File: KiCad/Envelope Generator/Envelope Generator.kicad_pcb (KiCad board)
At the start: 2 copper layers, 66 parts, among them J1 Screw_Terminal_01x03, J2 Screw_Terminal_01x03, U1 TL074, U2 TL074, U3 TL074

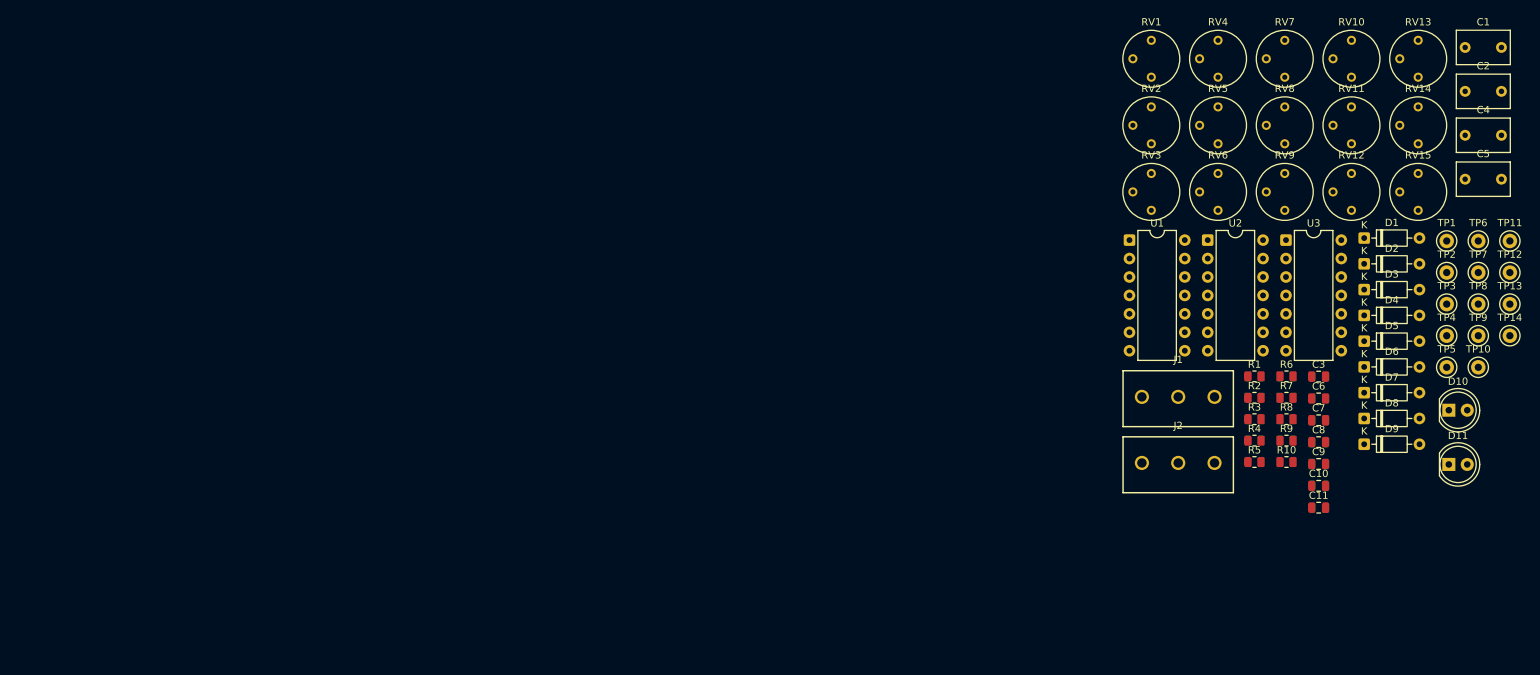
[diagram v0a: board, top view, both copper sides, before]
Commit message: envelope generator pcb layout done
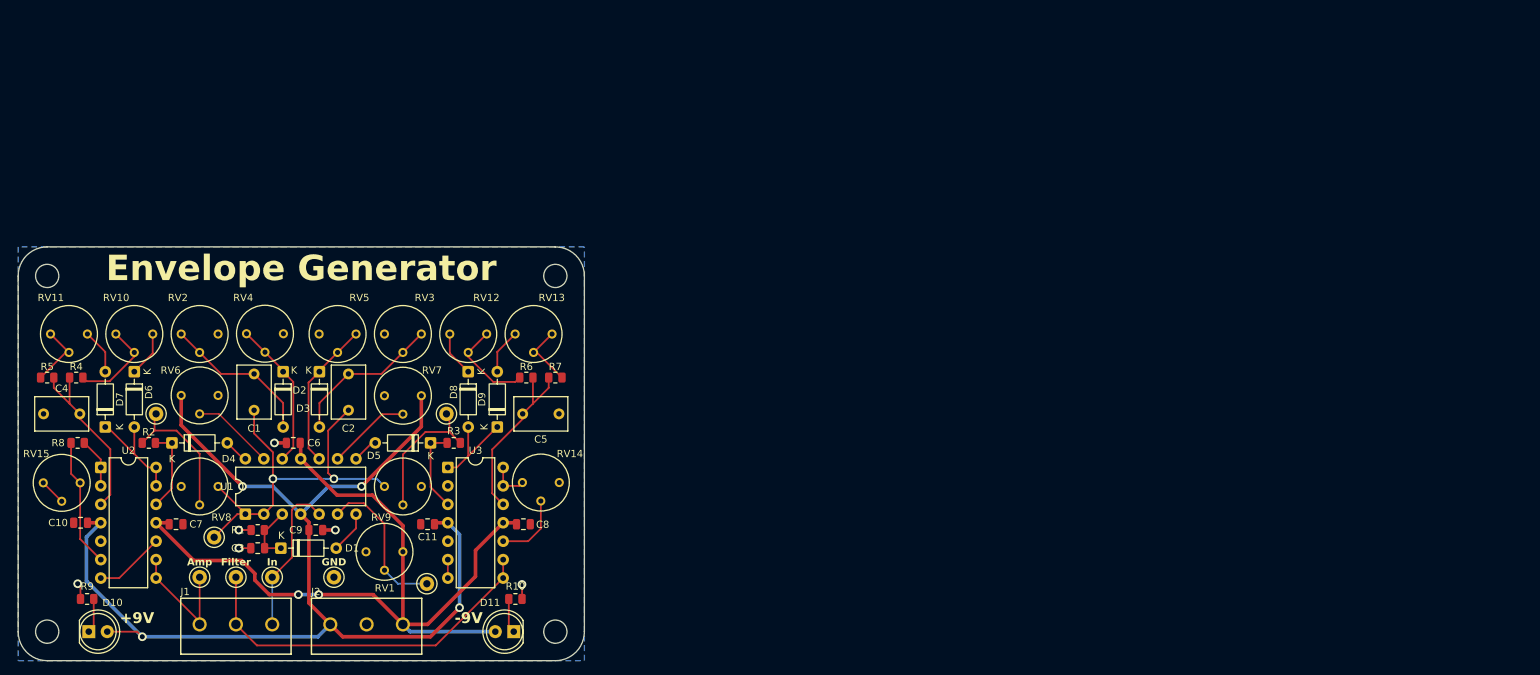
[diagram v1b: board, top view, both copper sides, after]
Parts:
- removed TP10, TP11, TP13, TP14, TP2, TP3: TestPoint_Small, TestPoint:TestPoint_Keystone_5000-5004_Miniature
- added H1: MountingHole, MountingHole:MountingHole_3.2mm_M3, F.Cu at (18.0, 66.0)
- added H2: MountingHole, MountingHole:MountingHole_3.2mm_M3, F.Cu at (18.0, 115.0)
- added H3: MountingHole, MountingHole:MountingHole_3.2mm_M3, F.Cu at (88.0, 115.0)
- added H4: MountingHole, MountingHole:MountingHole_3.2mm_M3, F.Cu at (88.0, 66.0)
- R10, R9: value R_US -> 1k
- moved C4 199.5 mm to (17.5, 85.0)
- moved D10 189.8 mm to (23.7, 115.0)
- moved RV15 188.1 mm to (22.5, 94.5), turned to 90 degrees
- moved TP7 181.1 mm to (39.0, 107.5)
- moved TP5 177.9 mm to (33.0, 85.0)
- moved RV11 176.1 mm to (23.5, 74.0), turned to 90 degrees
- moved TP8 175.2 mm to (44.0, 107.5)
- moved C1 174.1 mm to (46.5, 84.5), turned to 90 degrees
- moved D7 173.5 mm to (26.0, 86.8), turned to 90 degrees
- moved TP4 172.0 mm to (41.0, 102.0)
- moved C10 170.6 mm to (22.6, 100.0)
- moved TP9 169.4 mm to (49.0, 107.5)
- moved D6 169.4 mm to (30.0, 79.2), turned to -90 degrees
- moved RV10 168.9 mm to (32.5, 74.0), turned to 90 degrees
- moved TP12 167.3 mm to (57.5, 107.5)
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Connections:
- C4 pad 2: Net-(U2C-+) -> Net-(U2A-+)
- C5 pad 2: Net-(U2B-+) -> Net-(U3D-+)
- D11 pad 2: GND -> -9V
- J1 pad 1: /Envelope Generator/In -> /Envelope Generator/Amp Out
- J1 pad 2: /Envelope Generator/Amp Out -> /Envelope Generator/Filter Out
- J1 pad 3: /Envelope Generator/Filter Out -> /Envelope Generator/In
- R10 pad 2: -9V -> GND
- R4 pad 2: Net-(U2C-+) -> Net-(U2A-+)
- R5 pad 2: Net-(U2C-+) -> Net-(U2A-+)
- R6 pad 2: Net-(U2B-+) -> Net-(U3D-+)
- R7 pad 2: Net-(U2B-+) -> Net-(U3D-+)
- R8 pad 2: Net-(U3D--) -> Net-(U2B--)
- RV12 pad 1: Net-(D8-K) -> Net-(R6-Pad1)
- RV12 pad 3: Net-(R6-Pad1) -> Net-(D8-K)
- RV13 pad 1: Net-(D9-A) -> Net-(R7-Pad1)
- RV13 pad 3: Net-(R7-Pad1) -> Net-(D9-A)
- RV14 pad 1: /Envelope Generator/Unscaled Filter Out -> GND
- RV14 pad 2: Net-(U3B-+) -> Net-(U3C-+)
- RV14 pad 3: GND -> /Envelope Generator/Unscaled Filter Out
- RV15 pad 1: Net-(U3D--) -> Net-(U2B--)
- RV15 pad 2: Net-(U3C-+) -> Net-(U2C-+)
- RV15 pad 3: Net-(U3C-+) -> Net-(U2C-+)
- RV2 pad 1: Net-(D2-A) -> GND
- RV2 pad 3: GND -> Net-(D2-A)
- RV4 pad 1: Net-(D2-K) -> GND
- RV4 pad 3: GND -> Net-(D2-K)
- RV6 pad 1: +9V -> GND
- RV6 pad 2: Net-(U1C--) -> Net-(U1D--)
- RV6 pad 3: GND -> +9V
- RV7 pad 2: Net-(U1B--) -> Net-(U1C--)
- RV9 pad 1: /Envelope Generator/Normalized In -> GND
- RV9 pad 3: GND -> /Envelope Generator/Normalized In
- TP12 pad 1: /Envelope Generator/Unscaled Amp Out -> GND
- TP7 pad 1: /Envelope Generator/Amp Target Voltage -> /Envelope Generator/Amp Out
- TP8 pad 1: /Envelope Generator/Filter Target Voltage -> /Envelope Generator/Filter Out
- U1 pad 1: Net-(D1-A) -> /Envelope Generator/Normalized In
- U1 pad 10: Net-(D2-K) -> Net-(D3-K)
- U1 pad 12: Net-(D1-K) -> Net-(D2-K)
- U1 pad 13: /Envelope Generator/Normalized In -> Net-(U1D--)
- U1 pad 14: /Envelope Generator/Normalized In -> /Envelope Generator/Amp Burst
- U1 pad 2: /Envelope Generator/Input Comparator Ref -> /Envelope Generator/Normalized In
- U1 pad 3: /Envelope Generator/In -> Net-(D1-K)
- U1 pad 5: Net-(D3-K) -> /Envelope Generator/In
- U1 pad 6: Net-(U1B--) -> /Envelope Generator/Input Comparator Ref
- U1 pad 7: /Envelope Generator/Filter Burst -> Net-(D1-A)
- U1 pad 8: /Envelope Generator/Amp Burst -> /Envelope Generator/Filter Burst
- U2 pad 1: /Envelope Generator/Filter Target Voltage -> /Envelope Generator/Unscaled Amp Out
- U2 pad 2: /Envelope Generator/Filter Target Voltage -> /Envelope Generator/Unscaled Amp Out
- U2 pad 3: Net-(D5-K) -> Net-(U2A-+)
- U2 pad 5: Net-(U2B-+) -> GND
- U2 pad 6: /Envelope Generator/Unscaled Filter Out -> Net-(U2B--)
- U2 pad 7: /Envelope Generator/Unscaled Filter Out -> Net-(U2C-+)
- U2 pad 8: /Envelope Generator/Unscaled Amp Out -> /Envelope Generator/Amp Out
- U2 pad 9: /Envelope Generator/Unscaled Amp Out -> /Envelope Generator/Amp Out
- U3 pad 1: /Power/Thaw 3 -> /Envelope Generator/Filter Target Voltage
- U3 pad 12: GND -> Net-(U3D-+)
- U3 pad 13: Net-(U3D--) -> /Envelope Generator/Unscaled Filter Out
- U3 pad 14: Net-(U3C-+) -> /Envelope Generator/Unscaled Filter Out
- U3 pad 2: /Power/Thaw 3 -> /Envelope Generator/Filter Target Voltage
- U3 pad 3: GND -> Net-(D5-K)
- U3 pad 5: Net-(U3B-+) -> GND
- U3 pad 6: /Envelope Generator/Filter Out -> /Power/Thaw 3
- U3 pad 7: /Envelope Generator/Filter Out -> /Power/Thaw 3
- U3 pad 8: /Envelope Generator/Amp Out -> /Envelope Generator/Filter Out
- U3 pad 9: /Envelope Generator/Amp Out -> /Envelope Generator/Filter Out
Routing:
- net +9V: track 0.00 -> 156.1 mm, vias 0 -> 4
- net -9V: track 0.00 -> 112.8 mm, vias 0 -> 2
- net /Envelope Generator/Normalized In: track 0.00 -> 56.2 mm, vias 0 -> 2
- net /Envelope Generator/Filter Out: track 0.00 -> 50.9 mm
- net Net-(U3D-+): track 0.00 -> 24.9 mm
- net Net-(U2A-+): track 0.00 -> 24.8 mm
- net /Envelope Generator/In: track 0.00 -> 22.3 mm
- net Net-(D2-A): track 0.00 -> 21.8 mm
- net Net-(D3-A): track 0.00 -> 21.3 mm
- net /Envelope Generator/Input Comparator Ref: track 0.00 -> 21.3 mm
- net Net-(D2-K): track 0.00 -> 20.5 mm
- net Net-(D3-K): track 0.00 -> 20.5 mm
- net /Envelope Generator/Filter Sustain/Base Voltage: track 0.00 -> 19.4 mm
- net /Envelope Generator/Amp Sustain/Base Voltage: track 0.00 -> 19.4 mm
- net /Envelope Generator/Amp Out: track 0.00 -> 18.1 mm
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- added copper zone on B.Cu, net GND
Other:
- board outline added: 78 x 57 mm
- board text added: "+9V"
- board text added: "-9V"
- board text added: "Amp"
- board text added: "Envelope Generator"
- board text added: "Filter"
- board text added: "GND"
- board text added: "In"

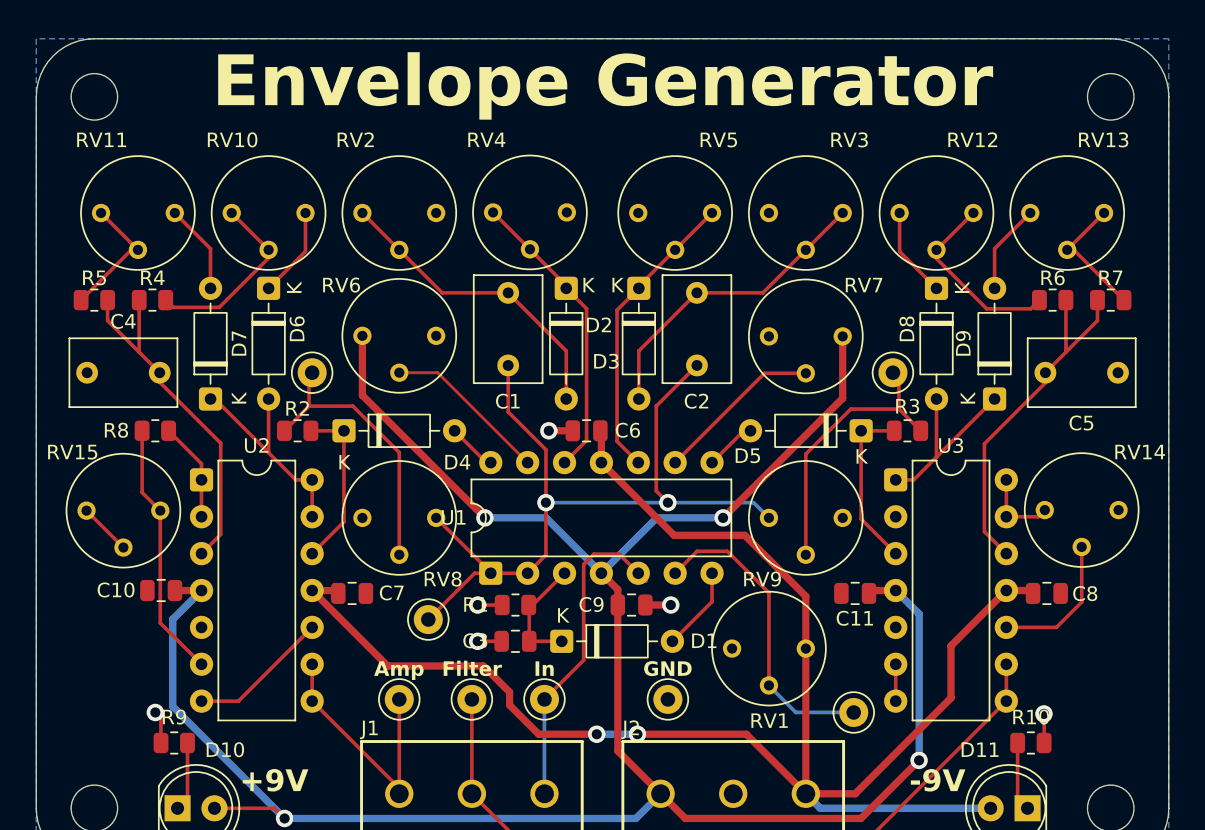
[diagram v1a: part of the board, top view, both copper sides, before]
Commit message: added informational silkscreen to envelope generator
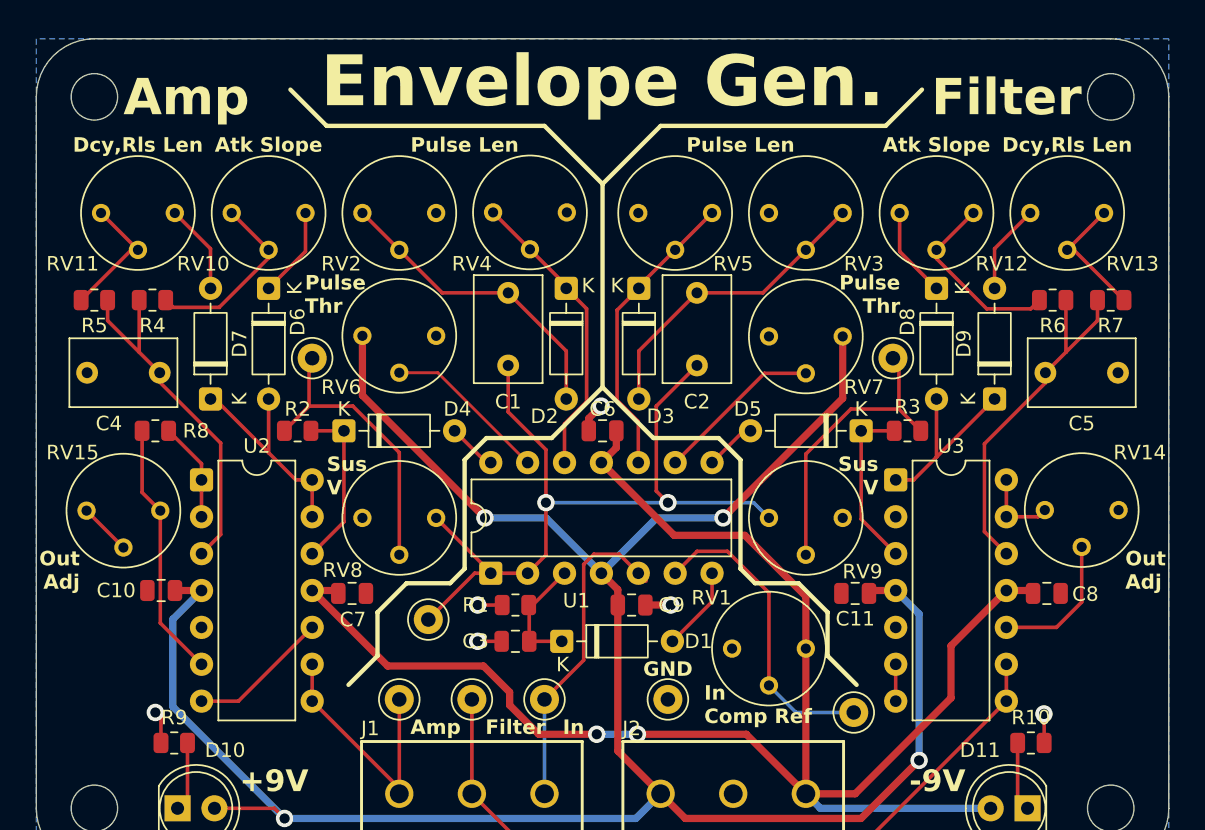
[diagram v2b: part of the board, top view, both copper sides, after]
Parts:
- moved C6 1.10 mm to (53.0, 89.0)
- moved TP5 1.00 mm to (33.0, 84.0)
- moved TP6 1.00 mm to (73.0, 84.0)
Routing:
- net /Envelope Generator/Filter Sustain/Base Voltage: track 19.4 -> 20.4 mm
- net /Envelope Generator/Amp Sustain/Base Voltage: track 19.4 -> 20.4 mm
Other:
- board text added: "Atk Slope"
- board text added: "Dcy,Rls Len"
- board text added: "Envelope Gen."
- board text added: "In Comp Ref"
- board text added: "Out Adj"
- board text added: "Pulse Len"
- board text added: "Pulse Thr"
- board text added: "Sus V"
- board text removed: "Envelope Generator"

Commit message: Update Envelope Generator.kicad_pcb
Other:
- board text added: "Envelope Gen"
- board text added: "Puls Thr"
- board text removed: "Envelope Gen."
- board text removed: "Pulse Thr"
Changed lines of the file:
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@@
 		(tags "Potentiometer vertical Bourns 3339P")
 		(property "Reference" "RV15"
-			(at 4 -6.04 180)
+			(at 4.5 -6.04 180)
 			(layer "F.SilkS")
 			(effects
@@
 		(tags "Potentiometer vertical Bourns 3339P")
 		(property "Reference" "RV6"
-			(at -3.54 -6.54 180)
+			(at 2.96 1.96 270)
 			(layer "F.SilkS")
 			(effects
@@
 		(tags "Potentiometer vertical Bourns 3339P")
 		(property "Reference" "RV5"
-			(at -3.5 1.46 180)
+			(at 4.5 -5.54 180)
 			(layer "F.SilkS")
 			(effects
@@
 		(tags "Potentiometer vertical Bourns 3339P")
 		(property "Reference" "RV2"
-			(at -3.5 -6.54 180)
+			(at 4.5 -5.54 180)
 			(layer "F.SilkS")
 			(effects
@@
 		(tags "Potentiometer vertical Bourns 3339P")
 		(property "Reference" "RV4"
-			(at -3.54 -6.54 180)
+			(at 4.46 0.21 180)
 			(layer "F.SilkS")
 			(effects
@@
 		(tags "Potentiometer vertical Bourns 3339P")
 		(property "Reference" "RV13"
-			(at -3.5 1.96 180)
+			(at 0 2.46 270)
 			(layer "F.SilkS")
 			(effects
@@
 		(tags "Potentiometer vertical Bourns 3339P")
 		(property "Reference" "RV11"
-			(at -3.5 -7.04 180)
+			(at 0 -7.54 270)
 			(layer "F.SilkS")
 			(effects
@@
 		(tags "Potentiometer vertical Bourns 3339P")
 		(property "Reference" "RV14"
-			(at 3.96 1.46 180)
+			(at 4.46 -0.04 180)
 			(layer "F.SilkS")
 			(effects
@@
 		(tags "Potentiometer vertical Bourns 3339P")
 		(property "Reference" "RV7"
-			(at -3.5 1.46 180)
+			(at 3 -7.04 270)
 			(layer "F.SilkS")
 			(effects
@@
 		(fp_text user "K"
 			(at 0 -1.8 90)
-			(layer "F.SilkS")
-			(effects
-				(font
-					(size 1 1)
-					(thickness 0.15)
-				)
-			)
-		)
-		(fp_text user "K"
-			(at 0 -1.8 90)
 			(layer "F.Fab")
 			(effects
@@
 		(tags "Potentiometer vertical Bourns 3339P")
 		(property "Reference" "RV12"
-			(at -3.5 1.96 180)
+			(at 6 -2.54 180)
 			(layer "F.SilkS")
 			(effects
@@
 			(layer "F.Fab")
 		)
-		(fp_text user "K"
-			(at 0 2 90)
-			(layer "F.SilkS")
-			(effects
-				(font
-					(size 1 1)
-					(thickness 0.15)
-				)
-			)
-		)
 		(fp_text user "${REFERENCE}"
 			(at 4.11 0 90)
@@
 		(tags "Potentiometer vertical Bourns 3339P")
 		(property "Reference" "RV1"
-			(at 3.5 -6.5 180)
+			(at 3 -6.5 180)
 			(layer "F.SilkS")
 			(effects
@@
 			(layer "F.Fab")
 		)
-		(fp_text user "K"
-			(at 0 -1.8 90)
-			(layer "F.SilkS")
-			(effects
-				(font
-					(size 1 1)
-					(thickness 0.15)
-				)
-			)
-		)
 		(fp_text user "${REFERENCE}"
 			(at 4.11 0 90)
@@
 		(tags "Potentiometer vertical Bourns 3339P")
 		(property "Reference" "RV3"
-			(at -3.5 1.46 180)
+			(at 4.5 0.46 180)
 			(layer "F.SilkS")
 			(effects
@@
 			(layer "F.Fab")
 		)
-		(fp_text user "K"
-			(at 0 -1.8 90)
-			(layer "F.SilkS")
-			(effects
-				(font
-					(size 1 1)
-					(thickness 0.15)
-				)
-			)
-		)
 		(fp_text user "${REFERENCE}"
 			(at 4.11 0 90)
@@
 		(tags "Potentiometer vertical Bourns 3339P")
 		(property "Reference" "RV10"
-			(at -3.5 -7.04 180)
+			(at 6 -2.54 180)
 			(layer "F.SilkS")
 			(effects
@@
 	)
 	(gr_line
-		(start 49 68)
-		(end 34 68)
-		(stroke
-			(width 0.3)
-			(type solid)
-		)
-		(layer "F.SilkS")
-	)
-	(gr_line
-		(start 49 68)
-		(end 53 72)
-		(stroke
-			(width 0.3)
-			(type solid)
-		)
-		(layer "F.SilkS")
-	)
-	(gr_line
 		(start 49.5 89.5)
 		(end 45 89.5)
@@
 	)
 	(gr_line
-		(start 53 72)
-		(end 53 86)
+		(start 53 68)
+		(end 34 68)
 		(stroke
 			(width 0.3)
@@
 	)
 	(gr_line
-		(start 53 72)
-		(end 57 68)
+		(start 53 68)
+		(end 53 86)
 		(stroke
 			(width 0.3)
@@
 	)
 	(gr_line
-		(start 53 86)
-		(end 56.5 89.5)
+		(start 53 68)
+		(end 72.5 68)
 		(stroke
 			(width 0.3)
@@
 	)
 	(gr_line
-		(start 57 68)
-		(end 72.5 68)
+		(start 53 86)
+		(end 56.5 89.5)
 		(stroke
 			(width 0.3)
@@
 		(layer "Edge.Cuts")
 	)
-	(gr_text "Pulse\nThr"
-		(at 32.5 81 0)
+	(gr_text "Sus\nV"
+		(at 34 93 0)
 		(layer "F.SilkS")
 		(effects
@@
 		)
 	)
-	(gr_text "Sus\nV"
-		(at 34 93.5 0)
+	(gr_text "In\nComp Ref"
+		(at 60 109.25 0)
 		(layer "F.SilkS")
 		(effects
@@
 		)
 	)
-	(gr_text "In\nComp Ref"
-		(at 60 109.25 0)
+	(gr_text "Puls\nThr"
+		(at 71 81 0)
 		(layer "F.SilkS")
 		(effects
@@
 	)
 	(gr_text "Out\nAdj"
-		(at 89 100 0)
+		(at 88 101.5 0)
 		(layer "F.SilkS")
 		(effects
@@
 	)
 	(gr_text "Out\nAdj"
-		(at 17 100 0)
+		(at 17.5 101.5 0)
 		(layer "F.SilkS")
 		(effects
@@
 		)
 	)
-	(gr_text "Sus\nV"
-		(at 72 93.5 0)
+	(gr_text "Puls\nThr"
+		(at 35 81 0)
 		(layer "F.SilkS")
 		(effects
@@
 		)
 	)
-	(gr_text "Pulse\nThr"
-		(at 73.5 81 0)
+	(gr_text "Sus\nV"
+		(at 72 93 0)
 		(layer "F.SilkS")
 		(effects
@@
 	)
 	(gr_text "Amp"
-		(at 20 67.5 0)
+		(at 21 66.5 0)
 		(layer "F.SilkS")
 		(effects
@@
 	)
 	(gr_text "Filter"
-		(at 86 67.5 0)
+		(at 86 66.5 0)
 		(layer "F.SilkS")
 		(effects
@@
 		)
 	)
-	(gr_text "Envelope Gen."
-		(at 53 67 0)
+	(gr_text "Envelope Gen"
+		(at 53 66.75 0)
 		(layer "F.SilkS")
 		(effects
 			(font
-				(size 3.5 3.5)
-				(thickness 0.7)
+				(size 3 3)
+				(thickness 0.6)
 				(bold yes)
 			)
@@
 		)
 		(min_thickness 0.25)
-		(fill
+		(fill yes
 			(thermal_gap 0.5)
 			(thermal_bridge_width 0.5)
